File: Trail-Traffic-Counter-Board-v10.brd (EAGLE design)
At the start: 50.8 x 44.5 mm, 46 parts

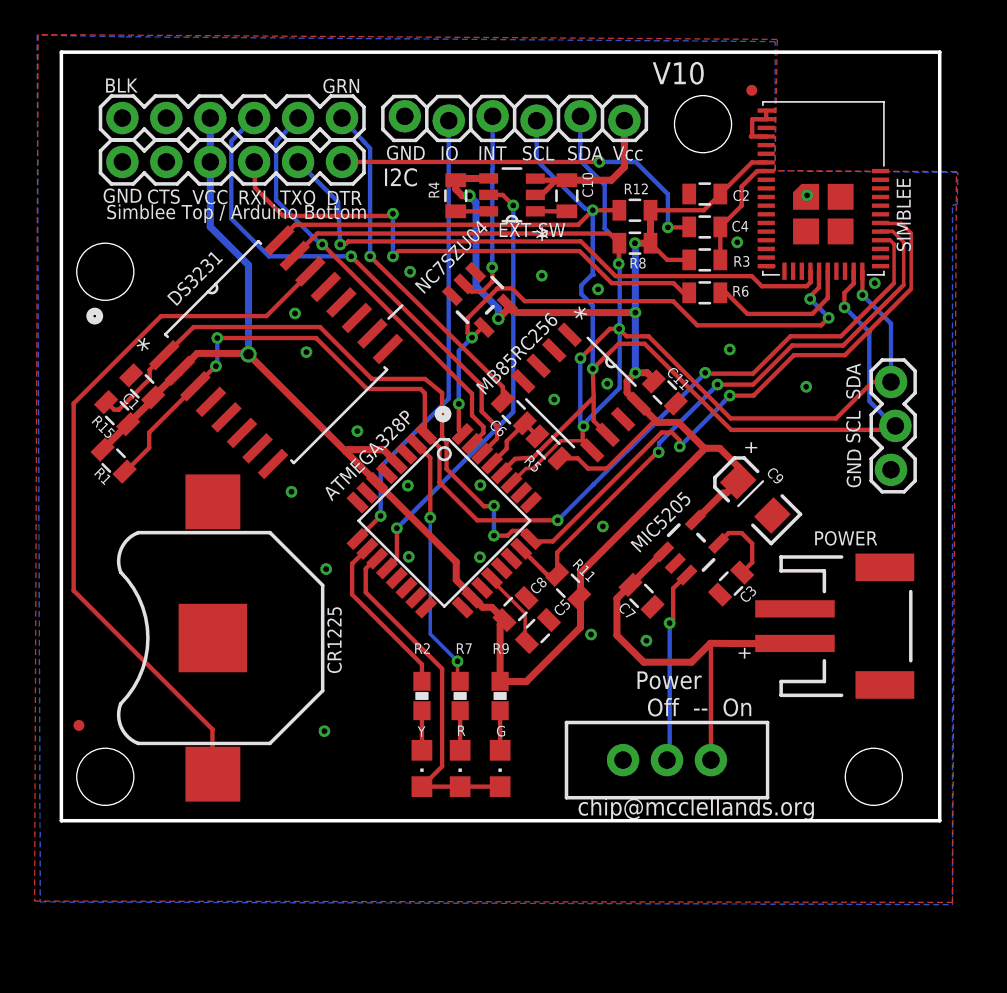
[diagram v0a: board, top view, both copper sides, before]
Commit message: Updated the design to include an on-off for the external i2c port
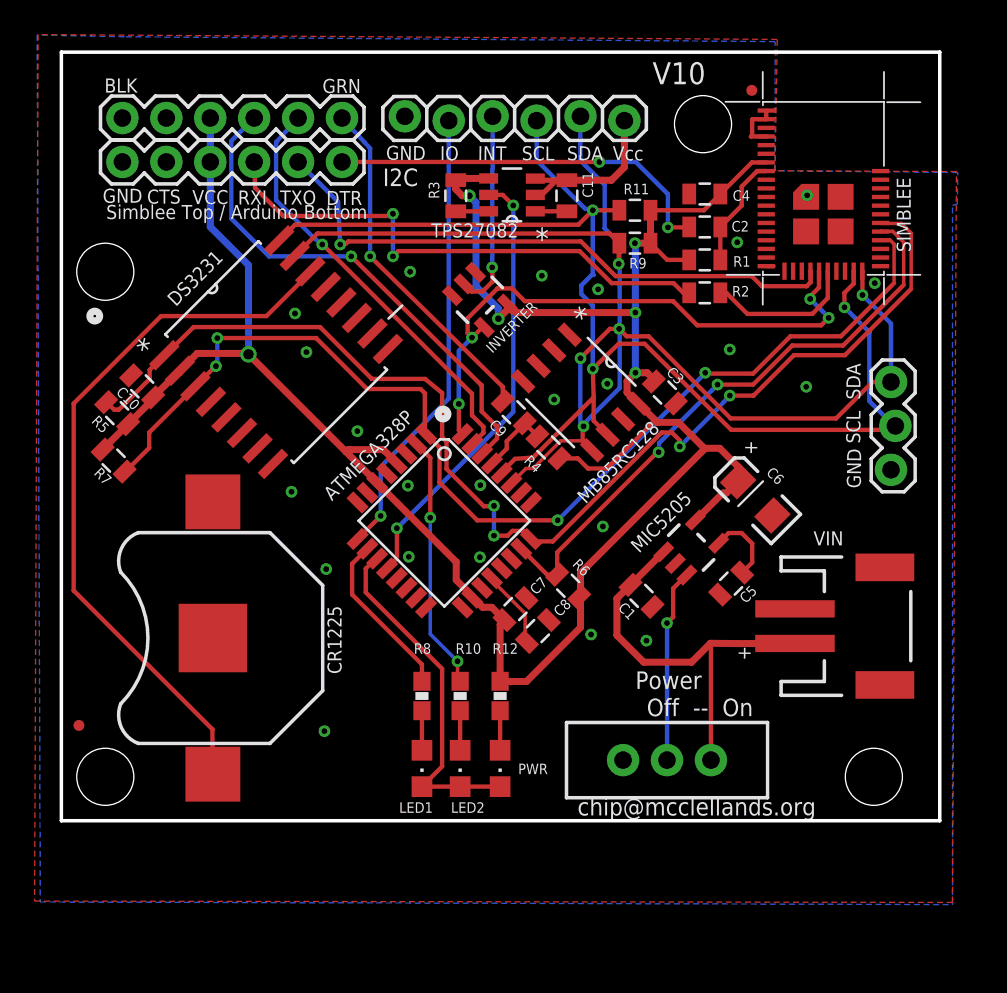
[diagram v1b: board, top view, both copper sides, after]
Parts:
- removed FTDI-S: FTDI_BASICPTH, SparkFun-Connectors:FTDI_BASIC
- removed R15: 10k, SparkFun-Passives:0805
- added JP8: STAND-OFF, SparkFun:STAND-OFF
- added R10: 330, SparkFun-Resistors:0603-RES
- C1: device SparkFun-Capacitors:0805 -> SparkFun-Passives:0805
- C11: value 0.1uF -> 1uF
- C2: value 0.1uF -> 10nF; device SparkFun-Capacitors:0805 -> SparkFun-Passives:0805
- C3: value 470pF -> 0.1uF; device SparkFun-Passives:0805 -> SparkFun-Capacitors:0805
- C4: value 10nF -> 0.1uF; device SparkFun-Passives:0805 -> SparkFun-Capacitors:0805
- C5: value 0.1uF -> 470pF; device SparkFun-Capacitors:0805 -> SparkFun-Passives:0805
- C6: value 0.1uF -> 10uF; device SparkFun-Capacitors:0805 -> SparkFun-Capacitors:EIA3216
- C7: value 1uF -> 0.1uF; device SparkFun-Passives:0805 -> SparkFun-Capacitors:0805
- C9: value 10uF -> 0.1uF; device SparkFun-Capacitors:EIA3216 -> SparkFun-Capacitors:0805
- JP4: value STAND-OFF -> FTDI_BASICPTH; device SparkFun:STAND-OFF -> SparkFun-Connectors:FTDI_BASIC
- R1: value 10k -> 10K
- R11: value 10k -> 4.7k; device SparkFun-Passives:0805 -> SparkFun-Resistors:0805
- R12, R8: value 4.7k -> 330; device SparkFun-Resistors:0805 -> SparkFun-Resistors:0603-RES
- R2: value 330 -> 1k; device SparkFun-Resistors:0603-RES -> SparkFun-Passives:0805
- R3: value 10K -> 150k
- R4: value 150k -> 10k
- R6: value 1k -> 10k
- R7: value 330 -> 10k; device SparkFun-Resistors:0603-RES -> SparkFun-Passives:0805
- R9: value 330 -> 4.7k; device SparkFun-Resistors:0603-RES -> SparkFun-Resistors:0805
- moved JP4 47.0 mm to (16.2, 38.1), turned to 180 degrees
- moved JP6 39.0 mm to (47.0, 2.54)
- moved R1 36.1 mm to (37.2, 32.4), turned to 180 degrees
- moved C1 31.3 mm to (33.6, 13.0), turned to 315 degrees
- moved R12 29.2 mm to (25.4, 7.21), turned to 90 degrees
- moved R8 28.9 mm to (20.9, 7.21), turned to 90 degrees
- moved R2 28.5 mm to (37.2, 30.5), turned to 0 degrees
- moved R9 27.3 mm to (33.2, 33.4), turned to 0 degrees
- moved C10 26.9 mm to (4.67, 25.1), turned to 135 degrees
- moved R5 25.0 mm to (3.23, 23.6)
- moved R7 24.2 mm to (3.02, 20.8), turned to 135 degrees
- moved R11 22.1 mm to (33.2, 35.3), turned to 0 degrees
- moved R6 18.7 mm to (29.3, 13.6), turned to 315 degrees
- moved R4 15.5 mm to (28.2, 21.6), turned to 315 degrees
- moved R3 14.9 mm to (22.8, 36.1), turned to 90 degrees
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- renumbered EXT-SW to TPS27082, FTDI-SIMBLEE-TOP-ARDUINO-BOTTOM to JP5, G to PWR, JP1 to $1_29_$_2016-08-26_17-19-35, JP3 to JP7, MB85RC256 to MB85RC128, NC7SZU04 to INVERTER, POWER to VIN, PWR-ON-OFF to S1, R to LED2, Y to LED1
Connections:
- net !RESET: now also C2.2, R1.1; no longer C4.2, R3.1
- net 32K: now also R5.1; no longer R15.1
- net AREF: now also C8.1; no longer C5.1
- net D6: now also R8.2; no longer R2.2
- net DTR: now also C9.1; no longer C6.1
- net DTR-S: now also C2.1, JP4.DTR; no longer C4.1, FTDI-S.DTR
- net EXTVCC: now also C11.1; no longer C10.1
- net GND: now also C4.2, C6.C, JP4.CTS, JP4.GND; no longer C2.2, C9.C, FTDI-S.CTS, FTDI-S.GND
- net INT/SQW: now also R7.1; no longer R1.1
- net N$1: now also R8.1; no longer R2.1
- net N$17: now also R2.2; no longer R6.2
- net N$2: now also C5.1; no longer C3.1
- net N$3: now also R10.2; no longer R7.2
- net N$38: now also R12.1; no longer R9.1
- net N$4: now also R10.1; no longer R7.1
- net N$5: now also R3.1; no longer R4.1
- net RESET: now also C9.2, R4.1; no longer C6.2, R5.1
- net RXI-S: now also JP4.TXO, R2.1; no longer FTDI-S.TXO, R6.1
- net SCL: now also R11.1; no longer R12.1
- net SDA: now also R9.1; no longer R8.1
- net TALK: now also R6.1; no longer R11.1
- net TXO-S: now also JP4.RXI; no longer FTDI-S.RXI
- net VCC: now also C10.1, C3.1, C4.1, C6.A, C7.1, JP4.VCC, R6.2, R7.2; no longer C1.1, C11.1, C2.1, C8.1, C9.A, FTDI-S.VCC, R15.2, R8.2
- net VRAW: now also C1.1; no longer C7.1

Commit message: Latest Design
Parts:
- removed $1_29_$_2016-08-26_17-19-35: (no value), SparkFun-Connectors:1X03_LOCK
- removed S1: (no value), SparkFun-Electromechanical:SWITCH-SPDT
- added BATT-I2C: (no value), SparkFun-Connectors:1X03_LOCK
- added C12: 10uF, SparkFun-Passives:0805
- added C13: 1uF, SparkFun-Capacitors:0805
- added D1: (no value), adafruit:SOD-523
- added NPN: MMBT2222A, SparkFun-DiscreteSemi:SOT23-3
- added POWER: (no value), SparkFun-Electromechanical:SWITCH-SPDT
- added R13: 100k, SparkFun-Passives:0805
- added R14: 4.7k, SparkFun-Resistors:0805
- added R15, R17: 100, SparkFun-Passives:0805
- added R16: 1k, SparkFun-Passives:0805
- added TRIGGER: SN74LVC1G17DBVRG4, Texas Instruments_By_element14_Batch_1:SOT95P280X145-5N
- moved C6 1.20 mm to (39.0, 18.3)
- moved VIN 1.19 mm to (46.1, 12.4)
- moved C5 0.18 mm to (38.6, 13.9)
- renumbered JP4 to FTDI-SIMBLEE, JP5 to FTDI-ARDUINO, MIC5205 to TC1015
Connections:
- removed net A2: ATMEGA328P.25
- removed net A7: ATMEGA328P.22
- new net HEARTBEAT: ATMEGA328P.22, R14.1, SIMBLEE.32
- new net N$14: R15.2, TRIGGER.4
- new net N$15: NPN.1, R16.1
- new net N$16: NPN.3, R17.2
- new net N$6: C13.2, D1.A, R13.1, R17.1, TRIGGER.2
- new net PWR-DWN: R16.2, SIMBLEE.31
- new net VIN: C1.1, D1.K, POWER.3, R13.2, TC1015.1, TRIGGER.5
- net !RESET: now also ATMEGA328P.25
- net ENABLE: now also R15.1; no longer S1.2
- net GND: now also BATT-I2C.1, C12.2, C13.1, NPN.2, TRIGGER.3; no longer $1_29_$_2016-08-26_17-19-35.1, S1.3
- net SCL: now also BATT-I2C.2; no longer $1_29_$_2016-08-26_17-19-35.2
- net SDA: now also BATT-I2C.3; no longer $1_29_$_2016-08-26_17-19-35.3
- net VCC: now also C12.1, R14.2
- net VRAW: now also POWER.2; no longer C1.1, S1.1, TC1015.1
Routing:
- net HEARTBEAT: track 0.00 -> 59.9 mm, vias 0 -> 5
- net VIN: track 0.00 -> 35.2 mm
- net N$16: track 0.00 -> 21.3 mm
- net !RESET: track 6.55 -> 26.4 mm, vias 0 -> 2
- net N$6: track 0.00 -> 13.4 mm
- net PWR-DWN: track 0.00 -> 12.3 mm, vias 0 -> 2
- net ENABLE: track 11.2 -> 4.07 mm, vias 1 -> 0
- net N$14: track 0.00 -> 5.45 mm
- net VRAW: track 24.1 -> 19.0 mm, vias 0 -> 1
- net SCL: track 78.9 -> 81.6 mm
- net N$15: track 0.00 -> 2.38 mm
- net N$2: track 4.37 -> 2.10 mm
- net TALK: track 34.9 -> 37.0 mm
- net INT/SQW: track 64.9 -> 67.0 mm
- net 32K: track 70.0 -> 71.9 mm
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- added copper zone on layer 1, net VCC
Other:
- board text added: "Trail Traffic Counter v10d 3-2-17"
- board text added: "V10d"
- board text removed: "Trail Traffic Counter v10 8-27-2016"
- board text removed: "V10"
